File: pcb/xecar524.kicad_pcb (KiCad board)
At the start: 2 copper layers, 62.8 x 89.4 mm, 48 parts, among them J1 JTAG, J2 ICSP, J3 Conn_02x02_Odd_Even, J4 TEST, U1 MCP1703A-3302_SOT89, U2 Atari_XE_Cartridge_Connector, U3 XC95144XL-TQ100, U4 SST39VF040, U5 PIC24FJ32GA004-I/PT, Y1 32768

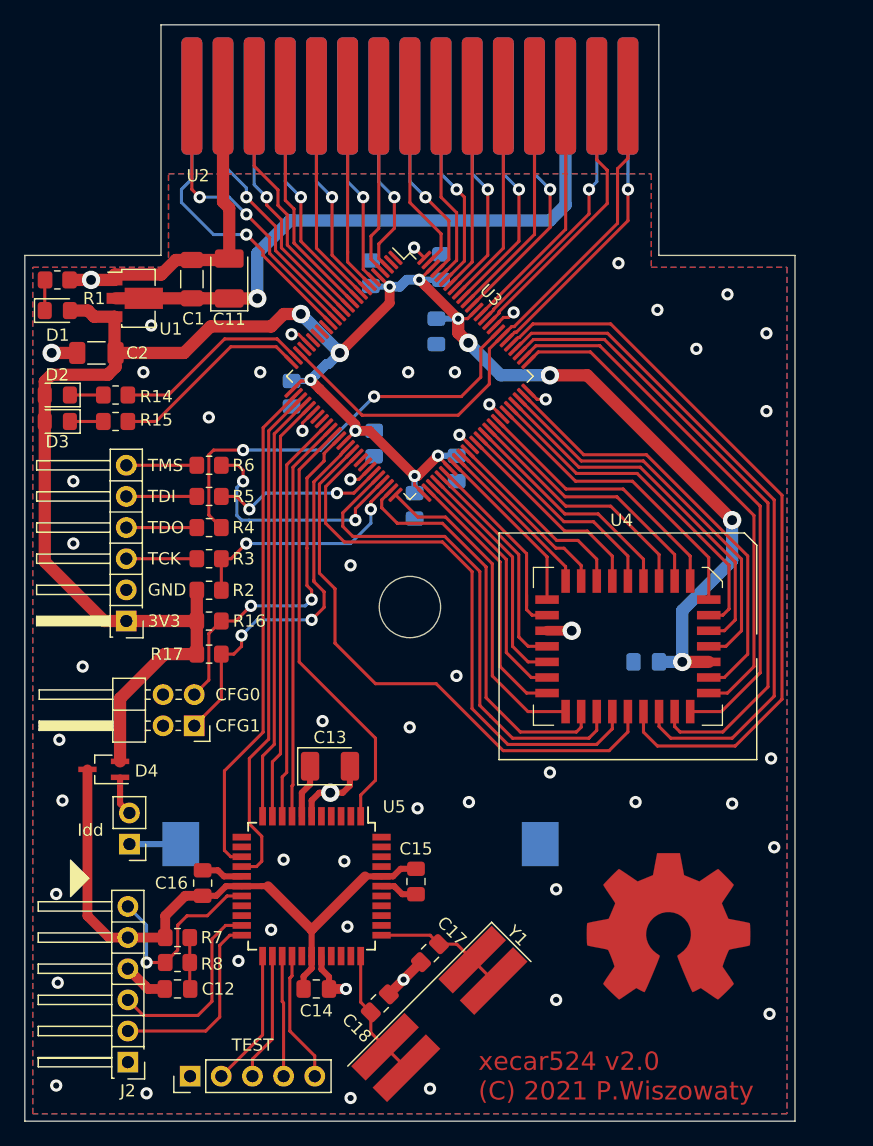
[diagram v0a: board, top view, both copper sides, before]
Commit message: PCB, PLD: Add one configuration jumper
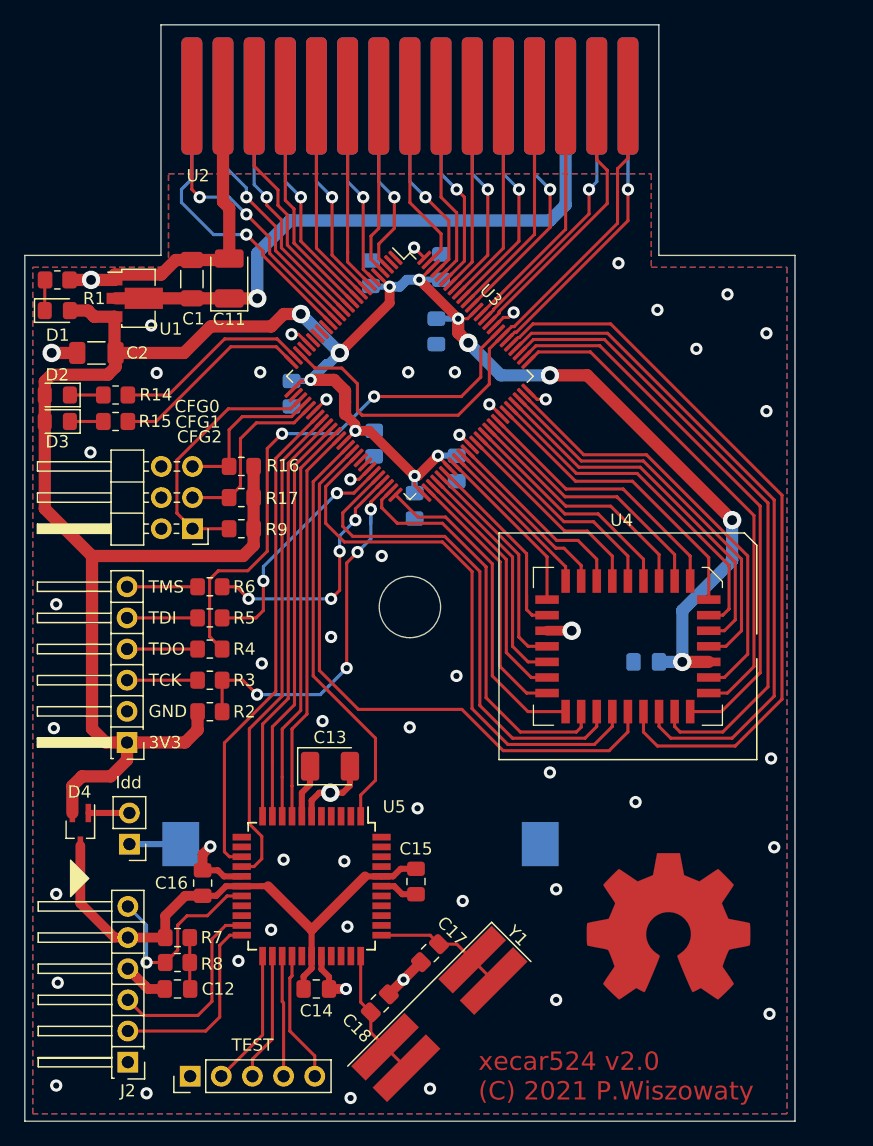
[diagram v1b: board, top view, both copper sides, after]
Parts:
- added R9: 10k, Resistor_SMD:R_0805_2012Metric_Pad1.20x1.40mm_HandSolder, F.Cu at (136.3, 85.8)
- J3: value Conn_02x02_Odd_Even -> CFG; footprint Connector_PinHeader_2.54mm:PinHeader_2x02_P2.54mm_Horizontal -> Connector_PinHeader_2.54mm:PinHeader_2x03_P2.54mm_Horizontal
- moved J3 16.1 mm to (132.3, 85.8)
- moved R17 13.0 mm to (136.3, 83.2)
- moved R16 12.9 mm to (136.3, 80.7), turned to 180 degrees
- moved J1 9.91 mm to (126.9, 103.2)
- moved R3 9.91 mm to (133.7, 98.1)
- moved R5 9.91 mm to (133.7, 93.1)
- moved R2 9.91 mm to (133.7, 100.7)
- moved R4 9.91 mm to (133.7, 95.6)
- moved R6 9.91 mm to (133.7, 90.5)
- moved D4 5.25 mm to (123.1, 110.3), turned to 270 degrees
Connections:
- J3 pad 1: CFG1 -> CFG2
- J3 pad 3: CFG0 -> CFG1
- R17 pad 1: +3V3 -> CFG1
- R17 pad 2: CFG1 -> +3V3
- U3 pad 27: PMWR -> Net-(U3-Pad27)
- U3 pad 28: PMCS1 -> CFG2
- U3 pad 29: PMRD -> CFG0
- U3 pad 30: PMD0 -> CFG1
- U3 pad 32: Net-(U3-Pad32) -> PMWR
- U3 pad 33: Net-(U3-Pad33) -> PMCS1
- U3 pad 34: PMD1 -> PMRD
- U3 pad 35: PMD2 -> PMD0
- U3 pad 36: PMD3 -> PMD1
- U3 pad 37: CFG0 -> PMD2
- U3 pad 39: CFG1 -> PMD3
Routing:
- net +3V3: track 184.1 -> 207.9 mm
- net CFG2: track 0.00 -> 21.2 mm
- net CFG1: track 31.8 -> 14.8 mm, vias 2 -> 0
- net CFG0: track 29.4 -> 13.0 mm, vias 2 -> 0
- net TCK: track 19.5 -> 31.4 mm, vias 2 -> 4
- net TDO: track 35.5 -> 44.3 mm
- net VDD: track 50.9 -> 44.6 mm
- net TDI: track 14.1 -> 19.4 mm
- net ROM_A11: track 47.1 -> 49.1 mm
- net GND: track 69.7 -> 71.6 mm, vias 56 -> 55
- net PMD3: track 35.4 -> 33.9 mm
- net Phi2: track 46.9 -> 48.2 mm
- net PMCS1: track 41.6 -> 40.5 mm
- net PMD0: track 34.5 -> 33.5 mm
- net PMRD: track 35.1 -> 34.0 mm
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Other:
- board text added: "CFG2"

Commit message: PCB, PLD: Add a connection between PLD and microcontroller
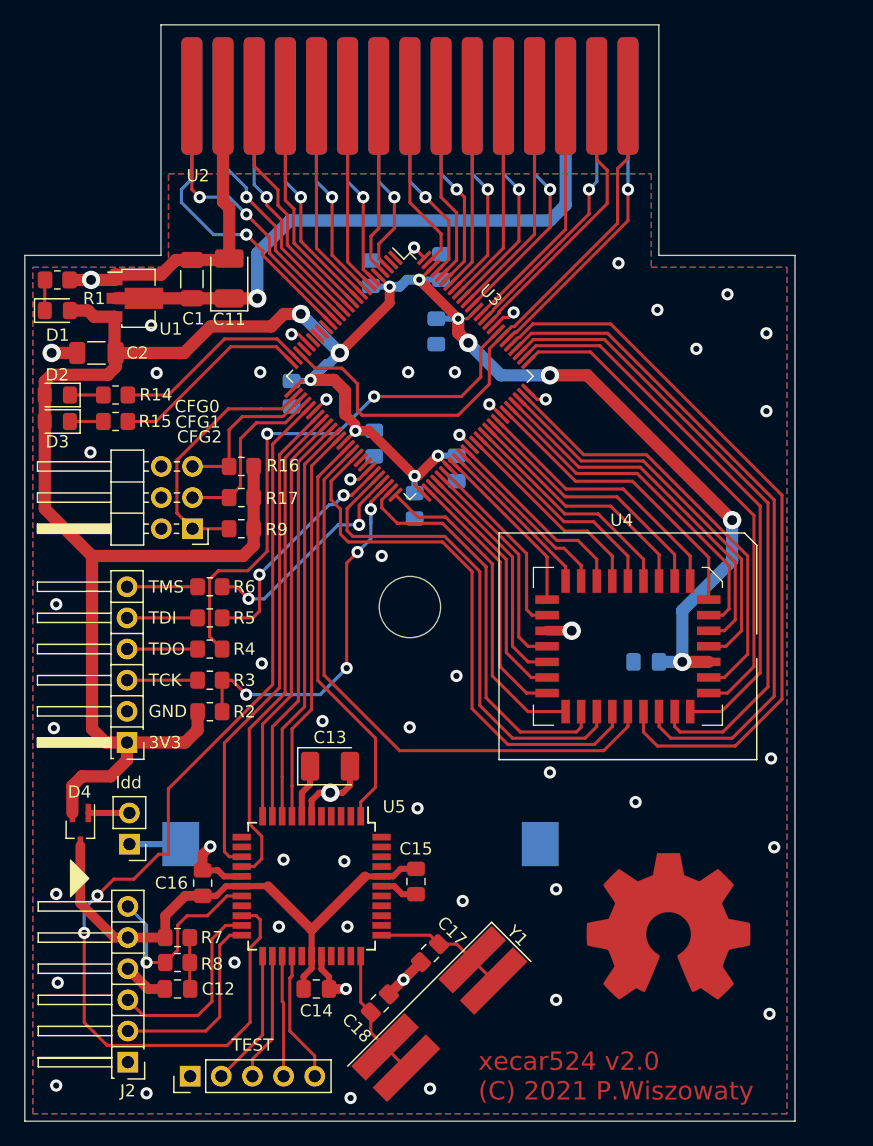
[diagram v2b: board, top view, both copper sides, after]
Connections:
- U3 pad 27: Net-(U3-Pad27) -> CFG2
- U3 pad 28: CFG2 -> CFG0
- U3 pad 29: CFG0 -> CFG1
- U3 pad 30: CFG1 -> MODE
- U5 pad 20: Net-(U5-Pad20) -> MODE
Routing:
- net MODE: track 0.00 -> 84.5 mm, vias 0 -> 2
- net TMS: track 20.6 -> 18.4 mm, vias 4 -> 2
- net TDO: track 44.3 -> 45.0 mm
- net ROM_A11: track 49.1 -> 48.5 mm
- net OE#: track 45.8 -> 45.2 mm
- net GND: vias 55 -> 54

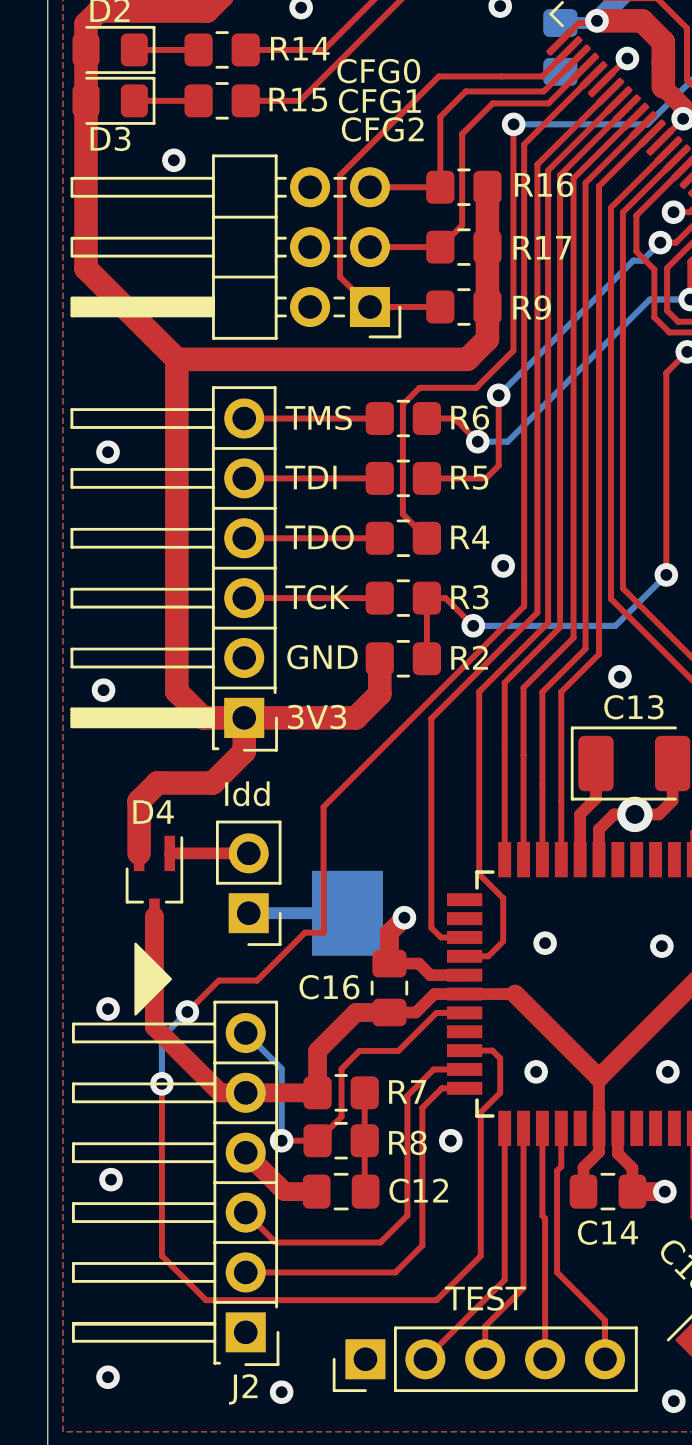
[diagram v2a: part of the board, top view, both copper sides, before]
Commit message: Tweak connections between PLD and uC
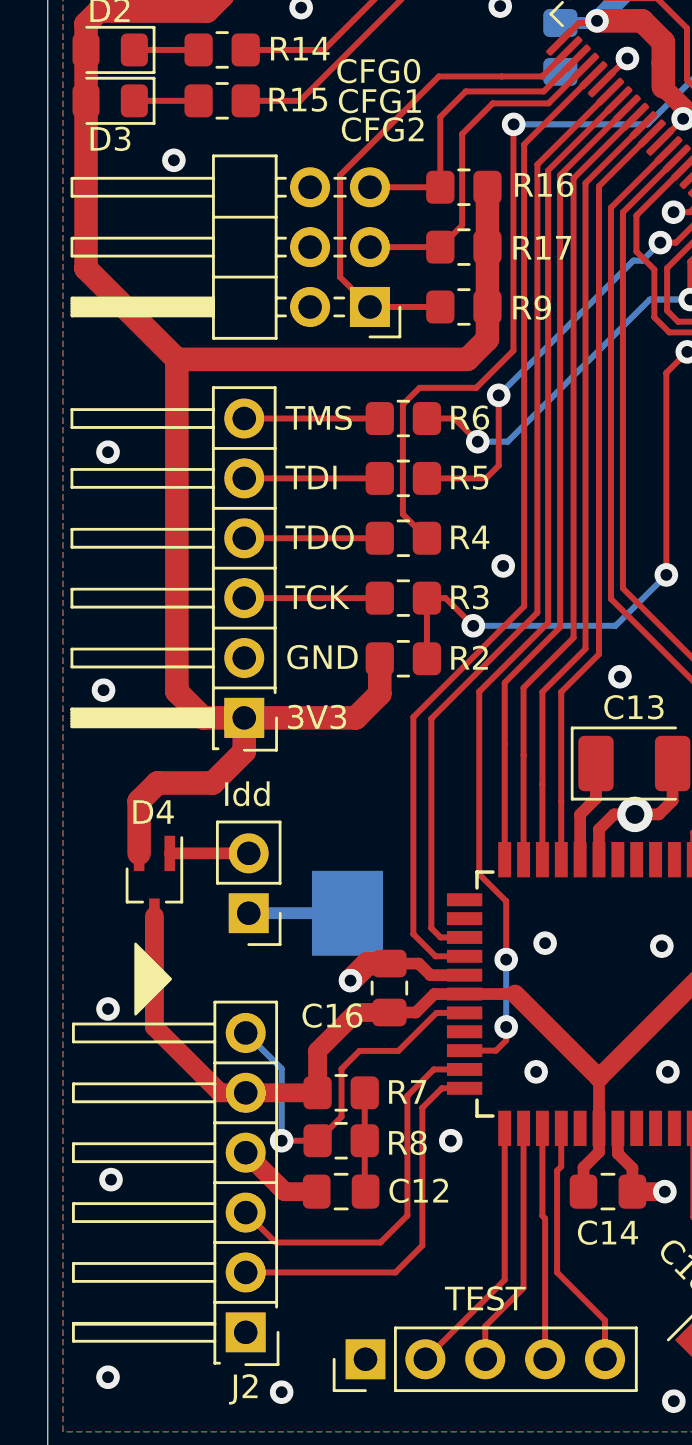
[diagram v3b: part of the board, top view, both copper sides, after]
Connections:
- U3 pad 30: MODE -> PMCS1
- U3 pad 33: PMCS1 -> MODE
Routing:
- net MODE: track 84.5 -> 44.8 mm
- net PMCS1: track 40.5 -> 42.2 mm
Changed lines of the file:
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@@
     (thickness 1.6)
     (drawings 22)
-    (tracks 766)
+    (tracks 752)
     (zones 0)
     (modules 49)
@@
     (add_net +3V3)
     (add_net +5V)
+    (add_net GND)
   )
   (net_class SmallPower ""
@@
     (uvia_dia 0.3)
     (uvia_drill 0.1)
-    (add_net GND)
   )
   (module Resistor_SMD:R_0805_2012Metric_Pad1.20x1.40mm_HandSolder (layer F.Cu)
@@
     (tags "capacitor handsolder")
     (attr smd)
-    (fp_text reference C16 (at 0 -2.54 180) (layer F.SilkS)
+    (fp_text reference C16 (at -1.2065 -2.413 180) (layer F.SilkS)
       (effects (font (size 1 1) (thickness 0.15)))
     )
@@
       (net 109 PMRD))
     (pad 33 smd roundrect (at -2.5 7.6625 315) (size 0.3 1.475) (layers F.Cu F.Paste F.Mask) (roundrect_rratio 0.25)
-      (net 105 PMCS1))
+      (net 128 MODE))
     (pad 32 smd roundrect (at -3 7.6625 315) (size 0.3 1.475) (layers F.Cu F.Paste F.Mask) (roundrect_rratio 0.25)
       (net 106 PMWR))
@@
       (net 3 GND))
     (pad 30 smd roundrect (at -4 7.6625 315) (size 0.3 1.475) (layers F.Cu F.Paste F.Mask) (roundrect_rratio 0.25)
-      (net 128 MODE))
+      (net 105 PMCS1))
     (pad 29 smd roundrect (at -4.5 7.6625 315) (size 0.3 1.475) (layers F.Cu F.Paste F.Mask) (roundrect_rratio 0.25)
       (net 83 CFG1))
@@
   (segment (start 130.005 123.317) (end 128.651 123.317) (width 0.8) (layer F.Cu) (net 3))
   (via (at 135.6995 121.158) (size 1) (drill 0.5) (layers F.Cu B.Cu) (net 3))
-  (segment (start 133.096 113.6435) (end 133.096 112.3315) (width 0.8) (layer F.Cu) (net 3))
-  (via (at 133.731 111.6965) (size 1) (drill 0.5) (layers F.Cu B.Cu) (net 3))
-  (segment (start 133.096 112.3315) (end 133.731 111.6965) (width 0.8) (layer F.Cu) (net 3))
   (via (at 143.1925 75.2475) (size 1) (drill 0.5) (layers F.Cu B.Cu) (net 3))
   (segment (start 143.162753 75.2475) (end 142.106921 76.303332) (width 0.254) (layer F.Cu) (net 3))
@@
   (via (at 147.701 88.011) (size 1) (drill 0.5) (layers F.Cu B.Cu) (net 3))
   (via (at 137.922 96.774) (size 1) (drill 0.5) (layers F.Cu B.Cu) (net 3))
+  (via (at 131.445 114.3635) (size 1) (drill 0.5) (layers F.Cu B.Cu) (net 3))
+  (segment (start 132.165 113.6435) (end 131.445 114.3635) (width 1) (layer F.Cu) (net 3))
+  (segment (start 133.096 113.6435) (end 132.165 113.6435) (width 1) (layer F.Cu) (net 3))
   (segment (start 153.296885 80.899526) (end 152.286 79.837) (width 0.254) (layer F.Cu) (net 4))
   (via (at 152.286 79.837) (size 1) (drill 0.5) (layers F.Cu B.Cu) (net 4))
@@
   (segment (start 134.976 118.135) (end 136.286 118.135) (width 0.254) (layer F.Cu) (net 103))
   (segment (start 133.858 119.253) (end 134.976 118.135) (width 0.254) (layer F.Cu) (net 103))
-  (segment (start 137.29 113.335) (end 136.286 113.335) (width 0.254) (layer F.Cu) (net 105))
-  (segment (start 137.922 110.871) (end 137.922 112.703) (width 0.254) (layer F.Cu) (net 105))
-  (segment (start 136.906 109.855) (end 137.922 110.871) (width 0.254) (layer F.Cu) (net 105))
-  (segment (start 137.922 112.703) (end 137.29 113.335) (width 0.254) (layer F.Cu) (net 105))
-  (segment (start 136.906 102.108) (end 136.906 109.855) (width 0.254) (layer F.Cu) (net 105))
-  (segment (start 139.827 99.187) (end 136.906 102.108) (width 0.254) (layer F.Cu) (net 105))
-  (segment (start 139.827 79.997466) (end 139.827 99.187) (width 0.254) (layer F.Cu) (net 105))
-  (segment (start 142.814027 77.010439) (end 139.827 79.997466) (width 0.254) (layer F.Cu) (net 105))
-  (segment (start 134.874 112.127) (end 135.282 112.535) (width 0.254) (layer F.Cu) (net 106))
+  (segment (start 135.052 113.335) (end 136.286 113.335) (width 0.254) (layer F.Cu) (net 105))
+  (segment (start 134.112 112.395) (end 135.052 113.335) (width 0.254) (layer F.Cu) (net 105))
+  (segment (start 134.112 103.1875) (end 134.112 112.395) (width 0.254) (layer F.Cu) (net 105))
+  (segment (start 138.811 98.4885) (end 134.112 103.1875) (width 0.254) (layer F.Cu) (net 105))
+  (segment (start 138.811 78.892146) (end 138.811 98.4885) (width 0.254) (layer F.Cu) (net 105))
+  (segment (start 141.753367 75.949779) (end 138.811 78.892146) (width 0.254) (layer F.Cu) (net 105))
+  (segment (start 136.906 102.108) (end 136.906 109.855) (width 0.254) (layer F.Cu) (net 128))
+  (segment (start 139.827 99.187) (end 136.906 102.108) (width 0.254) (layer F.Cu) (net 128))
+  (segment (start 139.827 79.997466) (end 139.827 99.187) (width 0.254) (layer F.Cu) (net 128))
+  (segment (start 142.814027 77.010439) (end 139.827 79.997466) (width 0.254) (layer F.Cu) (net 128))
   (segment (start 139.372991 98.752009) (end 134.874 103.251) (width 0.254) (layer F.Cu) (net 106))
   (segment (start 139.372991 79.744368) (end 139.372991 98.752009) (width 0.254) (layer F.Cu) (net 106))
-  (segment (start 134.874 103.251) (end 134.874 112.127) (width 0.254) (layer F.Cu) (net 106))
   (segment (start 142.460474 76.656885) (end 139.372991 79.744368) (width 0.254) (layer F.Cu) (net 106))
-  (segment (start 135.282 112.535) (end 136.286 112.535) (width 0.254) (layer F.Cu) (net 106))
   (segment (start 137.986 104.33) (end 137.986 109.235) (width 0.254) (layer F.Cu) (net 109))
   (segment (start 137.986 101.7275) (end 137.986 104.33) (width 0.254) (layer F.Cu) (net 109))
@@
   (segment (start 140.692707 74.889118) (end 139.572325 76.0095) (width 0.254) (layer F.Cu) (net 127))
   (segment (start 137.8585 76.0095) (end 135.1915 76.0095) (width 0.254) (layer F.Cu) (net 127))
-  (segment (start 141.753367 75.949779) (end 138.811 78.892146) (width 0.254) (layer F.Cu) (net 128))
-  (segment (start 138.811 78.892146) (end 138.811 80.9625) (width 0.254) (layer F.Cu) (net 128))
-  (segment (start 138.811 80.9625) (end 138.811 91.186) (width 0.254) (layer F.Cu) (net 128))
-  (segment (start 138.811 91.186) (end 138.811 97.409) (width 0.254) (layer F.Cu) (net 128))
-  (segment (start 138.811 97.409) (end 138.811 98.4885) (width 0.254) (layer F.Cu) (net 128))
-  (segment (start 138.811 98.4885) (end 130.302 106.9975) (width 0.254) (layer F.Cu) (net 128))
-  (segment (start 130.302 106.9975) (end 130.302 112.3315) (width 0.254) (layer F.Cu) (net 128))
-  (segment (start 129.512538 112.3315) (end 127.480538 114.3635) (width 0.254) (layer F.Cu) (net 128))
-  (segment (start 130.302 112.3315) (end 129.512538 112.3315) (width 0.254) (layer F.Cu) (net 128))
-  (segment (start 127.480538 114.3635) (end 125.857 114.3635) (width 0.254) (layer F.Cu) (net 128))
-  (via (at 124.5235 115.697) (size 1) (drill 0.5) (layers F.Cu B.Cu) (net 128))
-  (segment (start 125.857 114.3635) (end 124.5235 115.697) (width 0.254) (layer F.Cu) (net 128))
-  (segment (start 124.5235 115.697) (end 123.444 116.7765) (width 0.254) (layer B.Cu) (net 128))
-  (via (at 123.444 118.745) (size 1) (drill 0.5) (layers F.Cu B.Cu) (net 128))
-  (segment (start 123.444 116.7765) (end 123.444 118.745) (width 0.254) (layer B.Cu) (net 128))
-  (segment (start 137.4645 117.335) (end 136.286 117.335) (width 0.254) (layer F.Cu) (net 128))
-  (segment (start 136.9695 119.9515) (end 137.795 119.126) (width 0.254) (layer F.Cu) (net 128))
-  (segment (start 136.9695 126.0475) (end 136.9695 119.9515) (width 0.254) (layer F.Cu) (net 128))
-  (segment (start 135.093999 127.923001) (end 136.9695 126.0475) (width 0.254) (layer F.Cu) (net 128))
-  (segment (start 137.795 119.126) (end 137.795 117.6655) (width 0.254) (layer F.Cu) (net 128))
-  (segment (start 125.319501 127.923001) (end 135.093999 127.923001) (width 0.254) (layer F.Cu) (net 128))
-  (segment (start 123.444 126.0475) (end 125.319501 127.923001) (width 0.254) (layer F.Cu) (net 128))
-  (segment (start 137.795 117.6655) (end 137.4645 117.335) (width 0.254) (layer F.Cu) (net 128))
-  (segment (start 123.444 118.745) (end 123.444 126.0475) (width 0.254) (layer F.Cu) (net 128))
+  (segment (start 134.874 103.251) (end 134.874 112.141) (width 0.254) (layer F.Cu) (net 106))
+  (segment (start 135.268 112.535) (end 136.286 112.535) (width 0.254) (layer F.Cu) (net 106))
+  (segment (start 134.874 112.141) (end 135.268 112.535) (width 0.254) (layer F.Cu) (net 106))
+  (segment (start 136.906 109.855) (end 138.049 110.998) (width 0.254) (layer F.Cu) (net 128))
+  (via (at 138.049 113.4745) (size 1) (drill 0.5) (layers F.Cu B.Cu) (net 128))
+  (segment (start 138.049 110.998) (end 138.049 113.4745) (width 0.254) (layer F.Cu) (net 128))
+  (segment (start 138.049 113.4745) (end 138.049 116.332) (width 0.254) (layer B.Cu) (net 128))
+  (via (at 138.049 116.332) (size 1) (drill 0.5) (layers F.Cu B.Cu) (net 128))
+  (segment (start 138.049 116.9035) (end 138.049 116.332) (width 0.254) (layer F.Cu) (net 128))
+  (segment (start 137.6175 117.335) (end 138.049 116.9035) (width 0.254) (layer F.Cu) (net 128))
+  (segment (start 136.286 117.335) (end 137.6175 117.335) (width 0.254) (layer F.Cu) (net 128))
   (zone (net 3) (net_name GND) (layer B.Cu) (hatch edge 0.508)
     (connect_pads (clearance 0.508))

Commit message: PCB: Add connection for detecting power loss
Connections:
- U5 pad 23: TEST0 -> +3V3
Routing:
- net +3V3: track 207.9 -> 246.5 mm
- net TEST0: track 11.2 -> 0.00 mm
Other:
- board text added: "xecar524 v2.1 (C) 2021 P.Wiszowaty"
- board text removed: "xecar524 v2.0 (C) 2021 P.Wiszowaty"
